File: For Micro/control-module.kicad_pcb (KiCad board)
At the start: 2 copper layers, 23 parts, among them J1 For Light Sensor, J2 For Light Sensor, J3 From Solar Panel, J4 For Flow Module b, J5 For Flow Module a, U1 STR05, U2 ARDUINO_MICRO_SHIELD

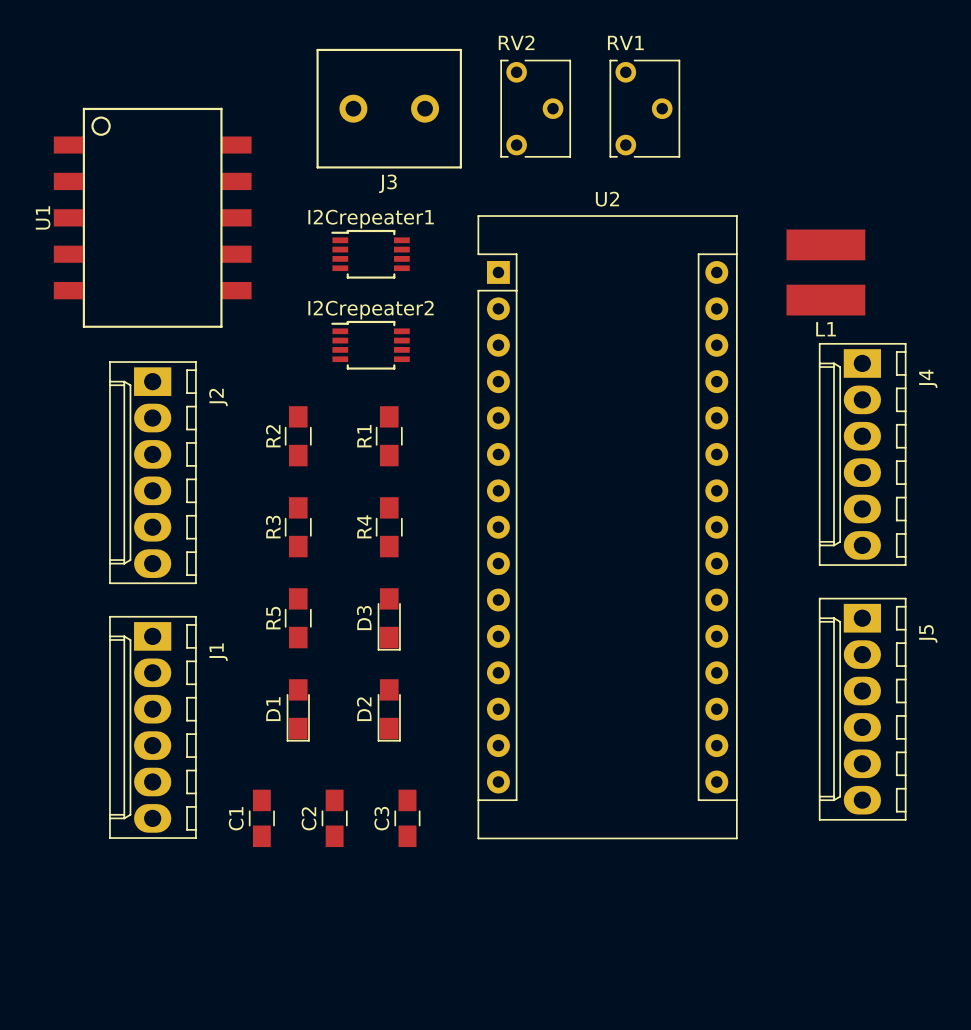
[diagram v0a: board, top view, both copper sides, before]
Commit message: Cleaned up control code, verified at this point. Added NMOS to Control CAD
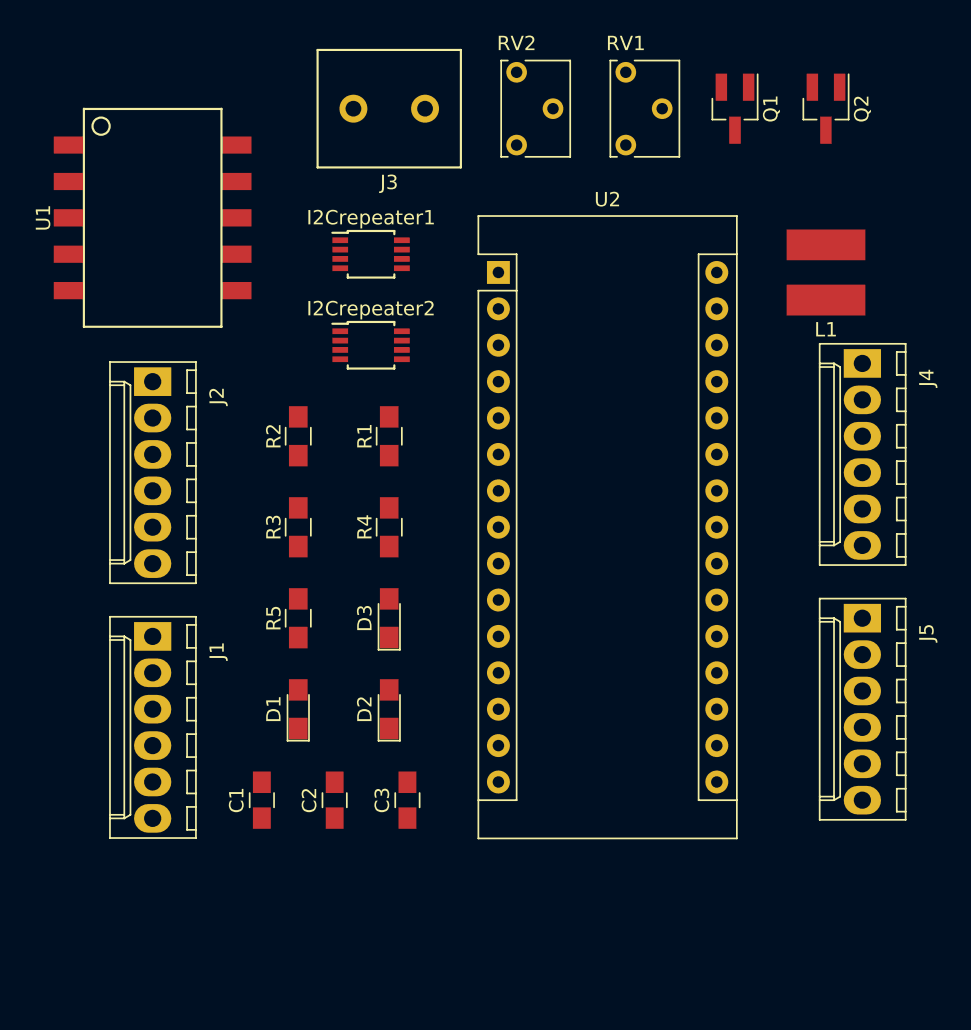
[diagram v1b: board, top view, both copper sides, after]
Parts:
- added Q1: NMOS, TO_SOT_Packages_SMD:SOT-23_Handsoldering, F.Cu at (134.6, 91.4)
- added Q2: NMOS, TO_SOT_Packages_SMD:SOT-23_Handsoldering, F.Cu at (141.0, 91.4)
- moved C1 1.27 mm to (101.6, 139.7)
- moved C2 1.27 mm to (106.7, 139.7)
- moved C3 1.27 mm to (111.8, 139.7)
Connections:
- U2 pad 4: INT -> INT/M
- U2 pad 5: DVI -> DVI/M
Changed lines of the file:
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@@
 (kicad_pcb (version 4) (host pcbnew 4.0.7)
   (general
-    (links 46)
-    (no_connects 46)
+    (links 50)
+    (no_connects 50)
     (area 0 0 0 0)
     (thickness 1.6)
@@
     (tracks 0)
     (zones 0)
-    (modules 23)
-    (nets 32)
+    (modules 25)
+    (nets 34)
   )
   (page A4)
@@
   (net 30 "Net-(U1-PadVADJ)")
   (net 31 EN)
+  (net 32 INT/M)
+  (net 33 DVI/M)
   (net_class Default "This is the default net class."
     (clearance 0.2)
@@
     (add_net DEBUG2)
     (add_net DVI)
+    (add_net DVI/M)
     (add_net EN)
     (add_net GND)
@@
     (add_net INPUT5)
     (add_net INT)
+    (add_net INT/M)
     (add_net "Net-(C3-Pad1)")
     (add_net "Net-(D1-Pad2)")
@@
   )
   (module Capacitors_SMD:C_0805_HandSoldering (layer F.Cu)
-    (at 101.6 140.97 90)
+    (at 101.6 139.7 90)
     (descr "Capacitor SMD 0805, hand soldering")
     (tags "capacitor 0805")
@@
   )
   (module Capacitors_SMD:C_0805_HandSoldering (layer F.Cu)
-    (at 106.68 140.97 90)
+    (at 106.68 139.7 90)
     (descr "Capacitor SMD 0805, hand soldering")
     (tags "capacitor 0805")
@@
   )
   (module Capacitors_SMD:C_0805_HandSoldering (layer F.Cu)
-    (at 111.76 140.97 90)
+    (at 111.76 139.7 90)
     (descr "Capacitor SMD 0805, hand soldering")
     (tags "capacitor 0805")
@@
     (pad 19 thru_hole oval (at 15.24 27.94) (size 1.6 1.6) (drill 0.8) (layers *.Cu *.Mask))
     (pad 4 thru_hole oval (at 0 7.62) (size 1.6 1.6) (drill 0.8) (layers *.Cu *.Mask)
-      (net 12 INT))
+      (net 32 INT/M))
     (pad 20 thru_hole oval (at 15.24 25.4) (size 1.6 1.6) (drill 0.8) (layers *.Cu *.Mask))
     (pad 5 thru_hole oval (at 0 10.16) (size 1.6 1.6) (drill 0.8) (layers *.Cu *.Mask)
-      (net 15 DVI))
+      (net 33 DVI/M))
     (pad 21 thru_hole oval (at 15.24 22.86) (size 1.6 1.6) (drill 0.8) (layers *.Cu *.Mask))
     (pad 6 thru_hole oval (at 0 12.7) (size 1.6 1.6) (drill 0.8) (layers *.Cu *.Mask)
@@
     (pad 16 thru_hole oval (at 15.24 35.56) (size 1.6 1.6) (drill 0.8) (layers *.Cu *.Mask))
   )
+  (module TO_SOT_Packages_SMD:SOT-23_Handsoldering (layer F.Cu)
+    (at 134.62 91.44 270)
+    (descr "SOT-23, Handsoldering")
+    (tags SOT-23)
+    (attr smd)
+    (fp_text reference Q1 (at 0 -2.5 270) (layer F.SilkS)
+      (effects (font (size 1 1) (thickness 0.15)))
+    )
+    (fp_text value NMOS (at 0 2.5 270) (layer F.Fab)
+      (effects (font (size 1 1) (thickness 0.15)))
+    )
+    (fp_text user %R (at 0 0 360) (layer F.Fab)
+      (effects (font (size 0.5 0.5) (thickness 0.075)))
+    )
+    (fp_line (start 0.76 1.58) (end 0.76 0.65) (layer F.SilkS) (width 0.12))
+    (fp_line (start 0.76 -1.58) (end 0.76 -0.65) (layer F.SilkS) (width 0.12))
+    (fp_line (start -2.7 -1.75) (end 2.7 -1.75) (layer F.CrtYd) (width 0.05))
+    (fp_line (start 2.7 -1.75) (end 2.7 1.75) (layer F.CrtYd) (width 0.05))
+    (fp_line (start 2.7 1.75) (end -2.7 1.75) (layer F.CrtYd) (width 0.05))
+    (fp_line (start -2.7 1.75) (end -2.7 -1.75) (layer F.CrtYd) (width 0.05))
+    (fp_line (start 0.76 -1.58) (end -2.4 -1.58) (layer F.SilkS) (width 0.12))
+    (fp_line (start -0.7 -0.95) (end -0.7 1.5) (layer F.Fab) (width 0.1))
+    (fp_line (start -0.15 -1.52) (end 0.7 -1.52) (layer F.Fab) (width 0.1))
+    (fp_line (start -0.7 -0.95) (end -0.15 -1.52) (layer F.Fab) (width 0.1))
+    (fp_line (start 0.7 -1.52) (end 0.7 1.52) (layer F.Fab) (width 0.1))
+    (fp_line (start -0.7 1.52) (end 0.7 1.52) (layer F.Fab) (width 0.1))
+    (fp_line (start 0.76 1.58) (end -0.7 1.58) (layer F.SilkS) (width 0.12))
+    (pad 1 smd rect (at -1.5 -0.95 270) (size 1.9 0.8) (layers F.Cu F.Paste F.Mask)
+      (net 12 INT))
+    (pad 2 smd rect (at -1.5 0.95 270) (size 1.9 0.8) (layers F.Cu F.Paste F.Mask)
+      (net 32 INT/M))
+    (pad 3 smd rect (at 1.5 0 270) (size 1.9 0.8) (layers F.Cu F.Paste F.Mask)
+      (net 2 GND))
+    (model ${KISYS3DMOD}/TO_SOT_Packages_SMD.3dshapes\SOT-23.wrl
+      (at (xyz 0 0 0))
+      (scale (xyz 1 1 1))
+      (rotate (xyz 0 0 0))
+    )
+  )
+  (module TO_SOT_Packages_SMD:SOT-23_Handsoldering (layer F.Cu)
+    (at 140.97 91.44 270)
+    (descr "SOT-23, Handsoldering")
+    (tags SOT-23)
+    (attr smd)
+    (fp_text reference Q2 (at 0 -2.5 270) (layer F.SilkS)
+      (effects (font (size 1 1) (thickness 0.15)))
+    )
+    (fp_text value NMOS (at 0 2.5 270) (layer F.Fab)
+      (effects (font (size 1 1) (thickness 0.15)))
+    )
+    (fp_text user %R (at 0 0 360) (layer F.Fab)
+      (effects (font (size 0.5 0.5) (thickness 0.075)))
+    )
+    (fp_line (start 0.76 1.58) (end 0.76 0.65) (layer F.SilkS) (width 0.12))
+    (fp_line (start 0.76 -1.58) (end 0.76 -0.65) (layer F.SilkS) (width 0.12))
+    (fp_line (start -2.7 -1.75) (end 2.7 -1.75) (layer F.CrtYd) (width 0.05))
+    (fp_line (start 2.7 -1.75) (end 2.7 1.75) (layer F.CrtYd) (width 0.05))
+    (fp_line (start 2.7 1.75) (end -2.7 1.75) (layer F.CrtYd) (width 0.05))
+    (fp_line (start -2.7 1.75) (end -2.7 -1.75) (layer F.CrtYd) (width 0.05))
+    (fp_line (start 0.76 -1.58) (end -2.4 -1.58) (layer F.SilkS) (width 0.12))
+    (fp_line (start -0.7 -0.95) (end -0.7 1.5) (layer F.Fab) (width 0.1))
+    (fp_line (start -0.15 -1.52) (end 0.7 -1.52) (layer F.Fab) (width 0.1))
+    (fp_line (start -0.7 -0.95) (end -0.15 -1.52) (layer F.Fab) (width 0.1))
+    (fp_line (start 0.7 -1.52) (end 0.7 1.52) (layer F.Fab) (width 0.1))
+    (fp_line (start -0.7 1.52) (end 0.7 1.52) (layer F.Fab) (width 0.1))
+    (fp_line (start 0.76 1.58) (end -0.7 1.58) (layer F.SilkS) (width 0.12))
+    (pad 1 smd rect (at -1.5 -0.95 270) (size 1.9 0.8) (layers F.Cu F.Paste F.Mask)
+      (net 15 DVI))
+    (pad 2 smd rect (at -1.5 0.95 270) (size 1.9 0.8) (layers F.Cu F.Paste F.Mask)
+      (net 33 DVI/M))
+    (pad 3 smd rect (at 1.5 0 270) (size 1.9 0.8) (layers F.Cu F.Paste F.Mask)
+      (net 2 GND))
+    (model ${KISYS3DMOD}/TO_SOT_Packages_SMD.3dshapes\SOT-23.wrl
+      (at (xyz 0 0 0))
+      (scale (xyz 1 1 1))
+      (rotate (xyz 0 0 0))
+    )
+  )
 )

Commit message: PCB for Control
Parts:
- added C4: 10uF, Capacitors_SMD:C_0805_HandSoldering, F.Cu at (104.1, 137.8)
- added D4: LED, LEDs:LED_0805_HandSoldering, F.Cu at (104.1, 128.9)
- added J6: For Flow Module a, valveteam-footprints:Molex_KK-6410-06_06x2.54mm_Straight, F.Cu at (142.2, 141.0)
- added JP1: Jumper_NO_Small, valveteam-footprints:SMD-solder-bridge, F.Cu at (120.7, 99.7)
- added JP2: Jumper_NO_Small, valveteam-footprints:SMD-solder-bridge, F.Cu at (128.3, 99.7)
- added JP3: Jumper_NO_Small, valveteam-footprints:SMD-solder-bridge, F.Cu at (124.5, 99.7)
- added L2: 6.8uH, valveteam-footprints:WURTH_INDUCTOR, F.Cu at (142.9, 92.1)
- added Q3: NMOS, TO_SOT_Packages_SMD:SOT-23_Handsoldering, F.Cu at (103.5, 149.2)
- added Q4: NMOS, TO_SOT_Packages_SMD:SOT-23_Handsoldering, F.Cu at (111.1, 149.2)
- added R6: 470, Resistors_SMD:R_0805_HandSoldering, F.Cu at (101.6, 118.7)
- added RV3: Trimmer Upper, Potentiometers:Potentiometer_Trimmer_Vishay_T73XX_Vertical, F.Cu at (144.1, 148.0)
- added U3: ARDUINO_MICRO_SHIELD, valveteam-footprints:ARDUINO_MICRO_SHIELD, F.Cu at (116.2, 104.5)
- C1, C2, C3: value 4.7uF -> 10uF
- J1: value For Light Sensor -> For Expansion
- J4: value For Flow Module b -> To Flow Module (F); footprint valveteam-footprints:Molex_KK-6410-06_06x2.54mm_Straight -> valveteam-footprints:TE_TERM
- J5: value For Flow Module a -> For Flow Module b
- L1: value 3.3uH -> 6.8uH
- R4, R5: value 150 -> 470
- U1: value STR05 -> TR_SERIES; footprint valveteam-footprints:STR05 -> valveteam-footprints:TR_Series
- U2: value ARDUINO_MICRO_SHIELD -> TR_SERIES; footprint valveteam-footprints:Arduino_Nano -> valveteam-footprints:TR_Series
- moved Q1 60.7 mm to (103.5, 143.5), turned to 0 degrees
- moved Q2 60.0 mm to (111.1, 143.5), turned to 0 degrees
- moved U2 26.4 mm to (94.6, 90.8)
- moved L1 11.9 mm to (135.9, 92.1)
- moved C1 10.6 mm to (110.5, 134.0), turned to 180 degrees
- moved D1 10.4 mm to (110.5, 125.1), turned to 180 degrees
- moved D2 10.4 mm to (104.1, 125.1), turned to 180 degrees
- moved R3 8.64 mm to (101.6, 112.4)
- moved R5 8.64 mm to (106.7, 118.7)
- moved I2Crepeater2 7.62 mm to (104.5, 102.0), turned to 90 degrees
- moved J4 6.48 mm to (142.2, 102.9)
- moved C2 6.25 mm to (104.1, 134.0), turned to 180 degrees
- moved U1 5.68 mm to (91.4, 104.1), turned to 90 degrees
- moved J1 5.24 mm to (92.7, 133.3)
- moved J2 4.02 mm to (92.7, 114.3)
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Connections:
- C2 pad 1: 12V -> Net-(C2-Pad1)
- C3 pad 1: Net-(C3-Pad1) -> 12V
- D1 pad 1: GND -> Net-(D1-Pad1)
- D1 pad 2: Net-(D1-Pad2) -> 12V
- D3 pad 1: GND -> Net-(D3-Pad1)
- D3 pad 2: Net-(D3-Pad2) -> VCC+5V
- J1 pad 1: VCC+3V -> VCC+EXP
- J2 pad 1: VCC+3V -> VCC+LS
- J4 pad 1: VCC+5V -> 12V
- J4 pad 2: INPUT2 -> GND
- J5 pad 2: Net-(J5-Pad2) -> INPUT2
- J5 pad 5: Net-(J5-Pad5) -> INPUT5
- L1 pad 2: Net-(L1-Pad2) -> Net-(C2-Pad1)
- Q1 pad 1: INT -> EN1
- Q1 pad 2: INT/M -> EN1/M
- Q2 pad 1: DVI -> EN2
- Q2 pad 2: DVI/M -> EN2/M
- R3 pad 1: 12V -> Net-(D1-Pad1)
- R3 pad 2: Net-(D1-Pad2) -> GND
- R5 pad 1: VCC+5V -> Net-(D3-Pad1)
- R5 pad 2: Net-(D3-Pad2) -> GND
- U1 pad VI: Net-(L1-Pad2) -> Net-(C2-Pad1)
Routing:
- net 12V: track 0.00 -> 146.6 mm, vias 0 -> 3
- net Net-(C2-Pad1): track 0.00 -> 104.7 mm, vias 0 -> 3
- net A0: track 0.00 -> 53.4 mm, vias 0 -> 1
- net Net-(C4-Pad1): track 0.00 -> 50.3 mm, vias 0 -> 2
- net A1: track 0.00 -> 47.7 mm, vias 0 -> 1
- net VCC+3V: track 0.00 -> 45.2 mm, vias 0 -> 2
- net 5V: track 0.00 -> 8.22 mm
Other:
- board outline added: 59.7 x 66 mm
- net class Default: trace_width 0.25 -> 0.4
